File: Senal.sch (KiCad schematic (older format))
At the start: 19 parts, among them IC1 AG849, IC2 AD5933, P1 GSG-RF-CONN, P2 GSG-RF-CONN, P3 CONN_02X04, P4 CONN_01X01, U1 AD8606

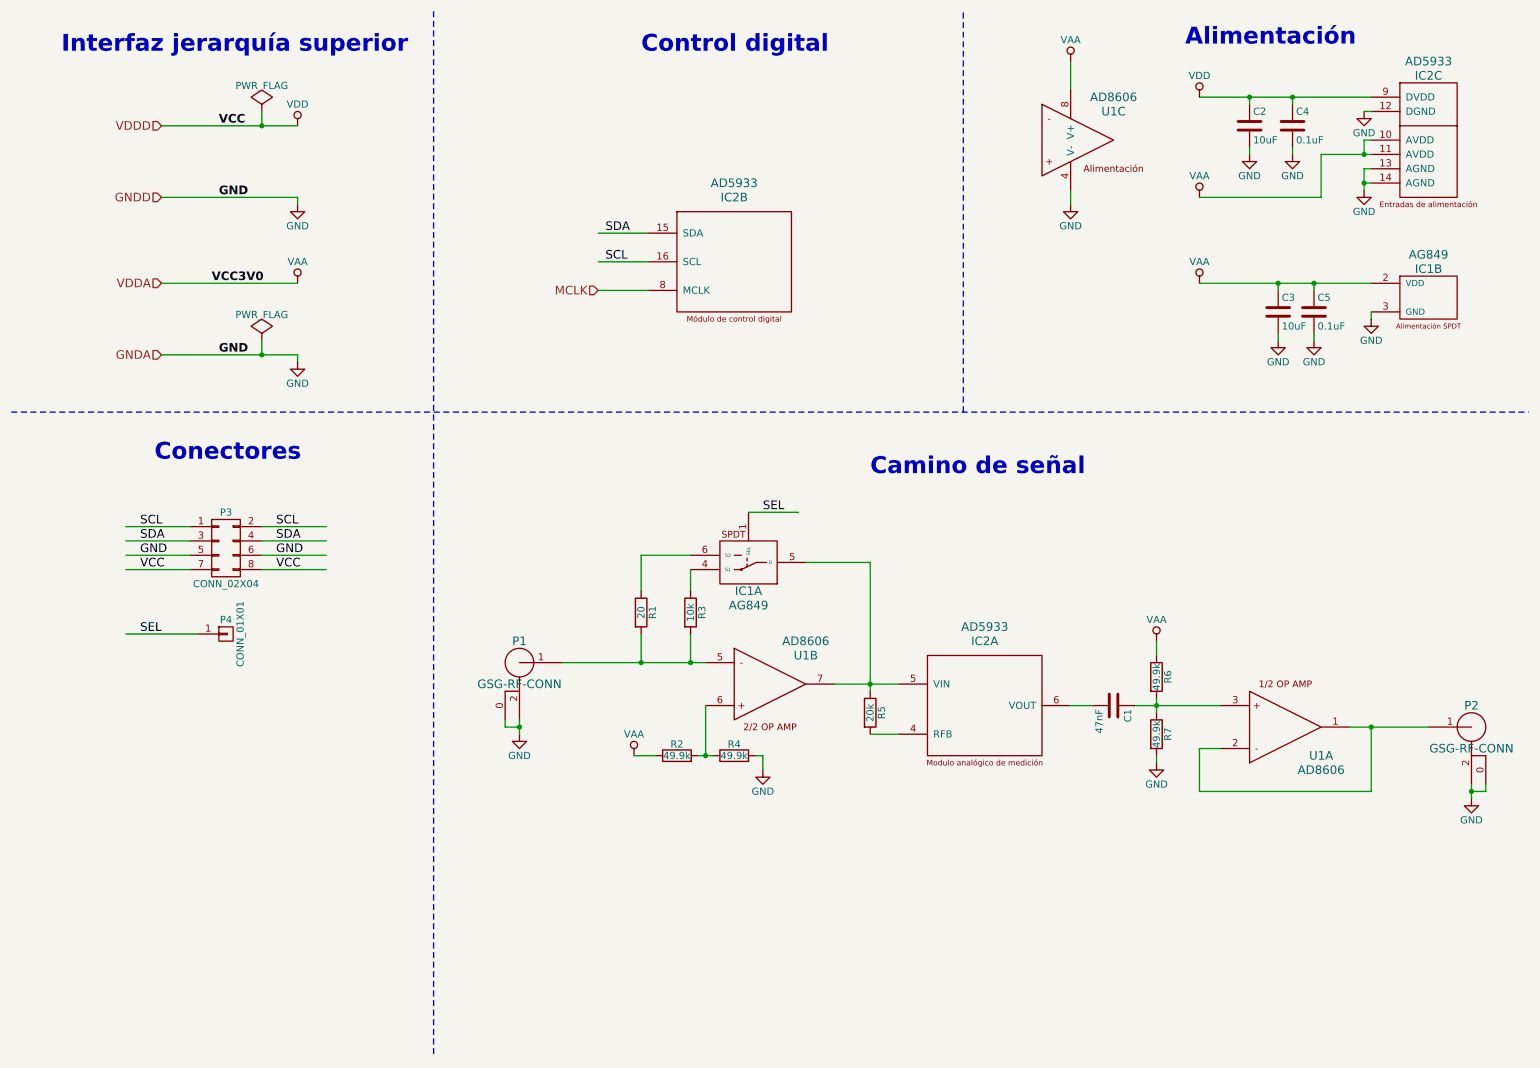
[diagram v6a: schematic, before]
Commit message: Se modificó el esquemático para cumplir con las correcciones propuestas. Resta modificar el rótulo y el símbolo de resistor. Agregar campos KiCost
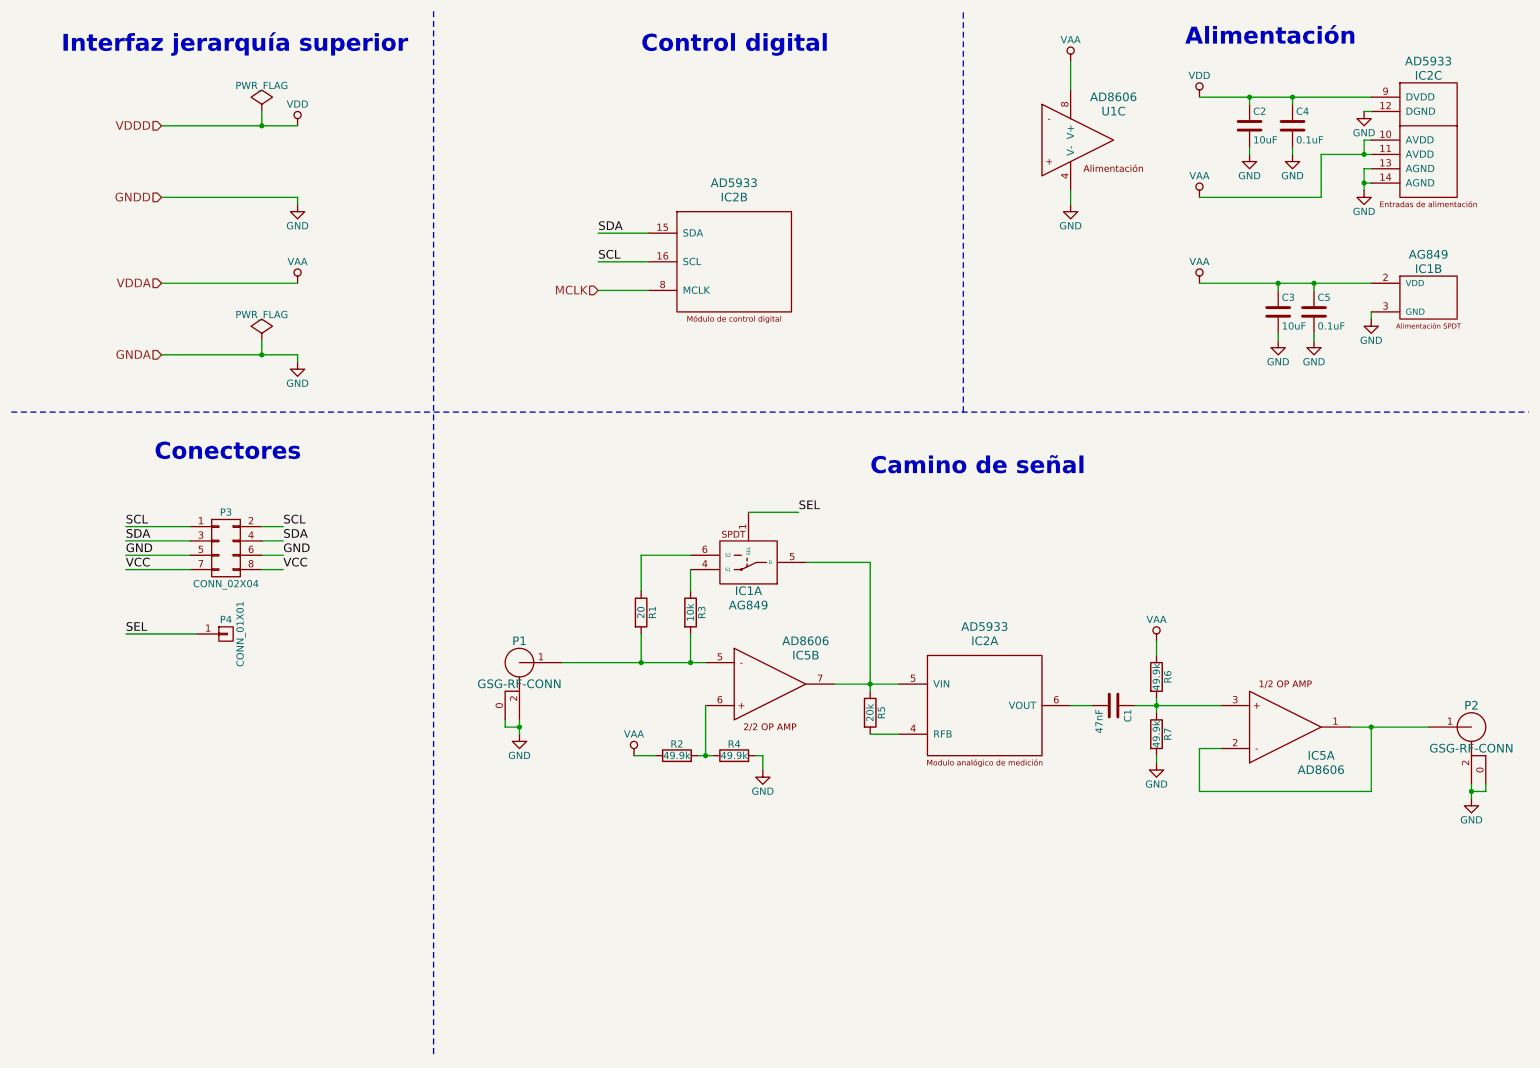
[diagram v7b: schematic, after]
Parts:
- C1, C2, C3, C4, C5: footprint Capacitors_SMD:C_0805 -> Capacitors_SMD:C_0603
- R1, R2, R3, R4, R5, R6, R7: footprint Resistors_SMD:R_0805 -> Resistors_SMD:R_0603
- renumbered U1 to IC5
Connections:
- net labels removed: VCC3V0
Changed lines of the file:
@@
 encoding utf-8
 Sheet 2 4
-Title ""
-Date ""
-Rev ""
-Comp ""
-Comment1 ""
-Comment2 ""
+Title "Medidor de impedancia (PMOD)"
+Date "2016-11-17"
+Rev "A"
+Comp "CESE - FIUBA"
+Comment1 "Autor: LAROSA, F."
+Comment2 "Revisor: GIGLIOTTI, E."
 Comment3 ""
 Comment4 ""
@@
 Text HLabel 4650 2450 0    60   Input ~ 0
 MCLK
-Text Label 2000 1300 0    60   ~ 12
-VCC
-Text Label 2000 1800 0    60   ~ 12
-GND
-Text Label 1950 2400 0    60   ~ 12
-VCC3V0
-Text Label 2000 2900 0    60   ~ 12
-GND
 $Comp
 L AD5933 IC2
@@
 F 0 "C2" H 9225 1400 50  0000 L CNN
 F 1 "10uF" H 9225 1200 50  0000 L CNN
-F 2 "Capacitors_SMD:C_0805" H 9238 1150 50  0001 C CNN
+F 2 "Capacitors_SMD:C_0603" H 9238 1150 50  0001 C CNN
 F 3 "" H 9200 1300 50  0000 C CNN
 	1    9200 1300
@@
 F 0 "C4" H 9525 1400 50  0000 L CNN
 F 1 "0.1uF" H 9525 1200 50  0000 L CNN
-F 2 "Capacitors_SMD:C_0805" H 9538 1150 50  0001 C CNN
+F 2 "Capacitors_SMD:C_0603" H 9538 1150 50  0001 C CNN
 F 3 "" H 9500 1300 50  0000 C CNN
 	1    9500 1300
@@
 F 0 "C3" H 9425 2700 50  0000 L CNN
 F 1 "10uF" H 9425 2500 50  0000 L CNN
-F 2 "Capacitors_SMD:C_0805" H 9438 2450 50  0001 C CNN
+F 2 "Capacitors_SMD:C_0603" H 9438 2450 50  0001 C CNN
 F 3 "" H 9400 2600 50  0000 C CNN
 	1    9400 2600
@@
 F 0 "C5" H 9675 2700 50  0000 L CNN
 F 1 "0.1uF" H 9675 2500 50  0000 L CNN
-F 2 "Capacitors_SMD:C_0805" H 9688 2450 50  0001 C CNN
+F 2 "Capacitors_SMD:C_0603" H 9688 2450 50  0001 C CNN
 F 3 "" H 9650 2600 50  0000 C CNN
 	1    9650 2600
@@
 $EndComp
 $Comp
-L AD8606 U1
+L AD8606 IC5
 U 1 1 582F8028
 P 9450 5500
-F 0 "U1" H 9700 5700 60  0000 C CNN
+F 0 "IC5" H 9700 5700 60  0000 C CNN
 F 1 "AD8606" H 9700 5800 60  0000 C CNN
 F 2 "Housings_SSOP:MSOP-8_3x3mm_Pitch0.65mm" H 9450 5500 60  0001 C CNN
@@
 $EndComp
 $Comp
-L AD8606 U1
+L AD8606 IC5
 U 2 1 582F8067
 P 5850 5200
-F 0 "U1" H 6100 5400 60  0000 C CNN
+F 0 "IC5" H 6100 5400 60  0000 C CNN
 F 1 "AD8606" H 6100 5500 60  0000 C CNN
 F 2 "Housings_SSOP:MSOP-8_3x3mm_Pitch0.65mm" H 5850 5200 60  0001 C CNN
@@
 F 0 "R5" V 6630 5400 50  0000 C CNN
 F 1 "20k" V 6550 5400 50  0000 C CNN
-F 2 "Resistors_SMD:R_0805" V 6480 5400 50  0001 C CNN
+F 2 "Resistors_SMD:R_0603" V 6480 5400 50  0001 C CNN
 F 3 "" H 6550 5400 50  0000 C CNN
 	1    6550 5400
@@
 F 0 "R6" V 8630 5150 50  0000 C CNN
 F 1 "49.9k" V 8550 5150 50  0000 C CNN
-F 2 "Resistors_SMD:R_0805" V 8480 5150 50  0001 C CNN
+F 2 "Resistors_SMD:R_0603" V 8480 5150 50  0001 C CNN
 F 3 "" H 8550 5150 50  0000 C CNN
 	1    8550 5150
@@
 F 0 "R7" V 8630 5550 50  0000 C CNN
 F 1 "49.9k" V 8550 5550 50  0000 C CNN
-F 2 "Resistors_SMD:R_0805" V 8480 5550 50  0001 C CNN
+F 2 "Resistors_SMD:R_0603" V 8480 5550 50  0001 C CNN
 F 3 "" H 8550 5550 50  0000 C CNN
 	1    8550 5550
@@
 F 0 "C1" H 8275 5450 50  0000 L CNN
 F 1 "47nF" H 8275 5250 50  0000 L CNN
-F 2 "Capacitors_SMD:C_0805" H 8288 5200 50  0001 C CNN
+F 2 "Capacitors_SMD:C_0603" H 8288 5200 50  0001 C CNN
 F 3 "" H 8250 5350 50  0000 C CNN
 	1    8250 5350
@@
 F 0 "R2" V 5280 5700 50  0000 C CNN
 F 1 "49.9k" V 5200 5700 50  0000 C CNN
-F 2 "Resistors_SMD:R_0805" V 5130 5700 50  0001 C CNN
+F 2 "Resistors_SMD:R_0603" V 5130 5700 50  0001 C CNN
 F 3 "" H 5200 5700 50  0000 C CNN
 	1    5200 5700
@@
 F 0 "R4" V 5680 5700 50  0000 C CNN
 F 1 "49.9k" V 5600 5700 50  0000 C CNN
-F 2 "Resistors_SMD:R_0805" V 5530 5700 50  0001 C CNN
+F 2 "Resistors_SMD:R_0603" V 5530 5700 50  0001 C CNN
 F 3 "" H 5600 5700 50  0000 C CNN
 	1    5600 5700
@@
 F 0 "R3" V 5375 4700 50  0000 C CNN
 F 1 "10k" V 5295 4700 50  0000 C CNN
-F 2 "Resistors_SMD:R_0805" V 5225 4700 50  0001 C CNN
+F 2 "Resistors_SMD:R_0603" V 5225 4700 50  0001 C CNN
 F 3 "" H 5295 4700 50  0000 C CNN
 	1    5295 4700
@@
 F 0 "R1" V 5030 4700 50  0000 C CNN
 F 1 "20" V 4950 4700 50  0000 C CNN
-F 2 "Resistors_SMD:R_0805" V 4880 4700 50  0001 C CNN
+F 2 "Resistors_SMD:R_0603" V 4880 4700 50  0001 C CNN
 F 3 "" H 4950 4700 50  0000 C CNN
 	1    4950 4700
 	1    0    0    -1
 $EndComp
-Text Label 5800 4000 0    60   ~ 0
+Text Label 6050 4000 0    60   ~ 0
 SEL
-Text Label 4700 2050 0    60   ~ 0
+Text Label 4650 2050 0    60   ~ 0
 SDA
-Text Label 4700 2250 0    60   ~ 0
+Text Label 4650 2250 0    60   ~ 0
 SCL
 Text Notes 8750 750  0    118  ~ 24
@@
 	5400 5350 5400 5700
 Wire Wire Line
-	4100 5550 4100 5450
+	4100 5450 4100 5550
 Wire Wire Line
 	4400 5050 5400 5050
@@
 	1800 4100 1350 4100
 Wire Wire Line
-	2300 4100 2750 4100
+	2300 4100 2450 4100
 Wire Wire Line
 	1350 4200 1800 4200
 Wire Wire Line
-	2300 4200 2750 4200
+	2300 4200 2450 4200
 Wire Wire Line
 	1350 4300 1800 4300
@@
 	1350 4400 1800 4400
 Wire Wire Line
-	2300 4300 2750 4300
-Wire Wire Line
-	2300 4400 2750 4400
-Text Label 1450 4100 0    60   ~ 0
+	2300 4300 2450 4300
+Wire Wire Line
+	2300 4400 2450 4400
+Text Label 1350 4100 0    60   ~ 0
 SCL
-Text Label 2400 4100 0    60   ~ 0
+Text Label 2450 4100 0    60   ~ 0
 SCL
-Text Label 1450 4200 0    60   ~ 0
+Text Label 1350 4200 0    60   ~ 0
 SDA
-Text Label 2400 4200 0    60   ~ 0
+Text Label 2450 4200 0    60   ~ 0
 SDA
-Text Label 1450 4300 0    60   ~ 0
+Text Label 1350 4300 0    60   ~ 0
 GND
-Text Label 2400 4300 0    60   ~ 0
+Text Label 2450 4300 0    60   ~ 0
 GND
-Text Label 1450 4400 0    60   ~ 0
+Text Label 1350 4400 0    60   ~ 0
 VCC
-Text Label 2400 4400 0    60   ~ 0
+Text Label 2450 4400 0    60   ~ 0
 VCC
 $Comp
@@
 Wire Wire Line
 	1850 4850 1350 4850
-Text Label 1450 4850 0    60   ~ 0
+Text Label 1350 4850 0    60   ~ 0
 SEL
 Text Notes 1550 3650 0    118  ~ 24
